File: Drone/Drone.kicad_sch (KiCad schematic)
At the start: 20 parts, among them IC1 STM32L412RBT6, J1 Conn_01x03_Pin, U1 ICP-10111, U2 BMI088

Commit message: new schematic
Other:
- added sheet Power (untitled.kicad_sch)
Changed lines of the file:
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@@
+		)
+	)
+	(sheet
+		(at 224.79 21.59)
+		(size 36.83 27.94)
+		(exclude_from_sim no)
+		(in_bom yes)
+		(on_board yes)
+		(dnp no)
+		(fields_autoplaced yes)
+		(stroke
+			(width 0.1524)
+			(type solid)
+		)
+		(fill
+			(color 0 0 0 0.0000)
+		)
+		(property "Sheetname" "Power"
+			(at 224.79 20.8784 0)
+			(effects
+				(font
+					(size 1.27 1.27)
+				)
+				(justify left bottom)
+			)
+		)
+		(property "Sheetfile" "untitled.kicad_sch"
+			(at 224.79 50.1146 0)
+			(effects
+				(font
+					(size 1.27 1.27)
+				)
+				(justify left top)
+			)
+		)
+		(instances
+			(project "Drone"
+				(path "/d78d7154-946a-48bf-8503-5b7bdc037515"
+					(page "2")
+				)
+			)
 		)
 	)

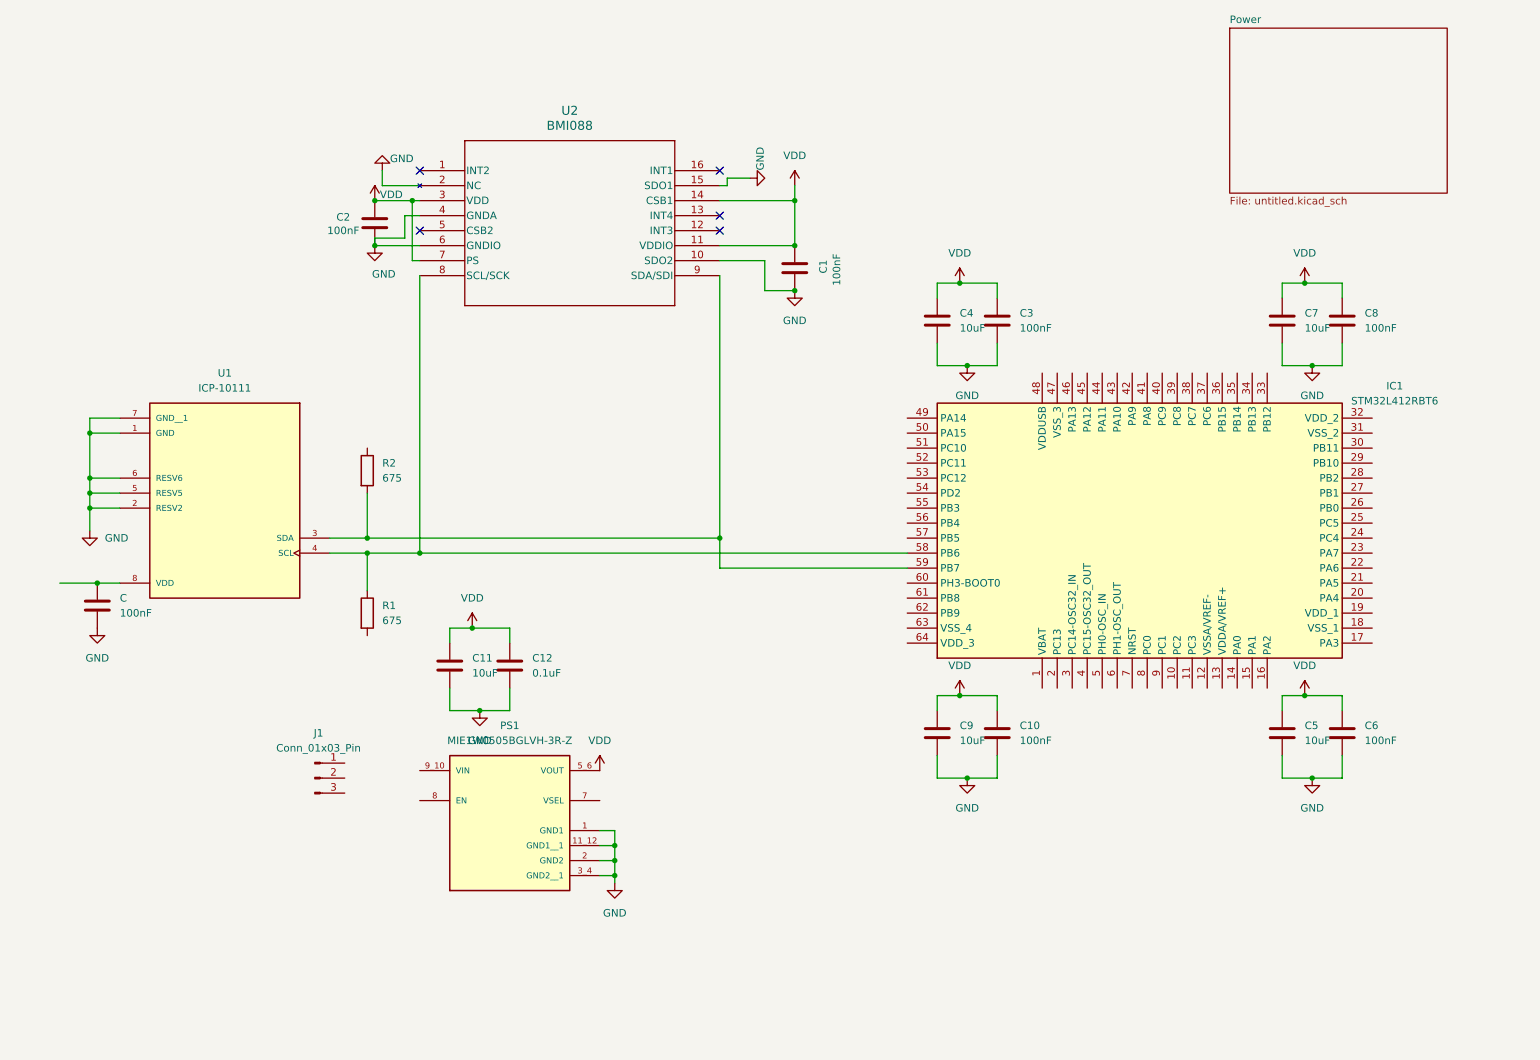
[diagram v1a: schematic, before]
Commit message: Added ICU and its connections to schematic
Added ICU and its connections to schematic
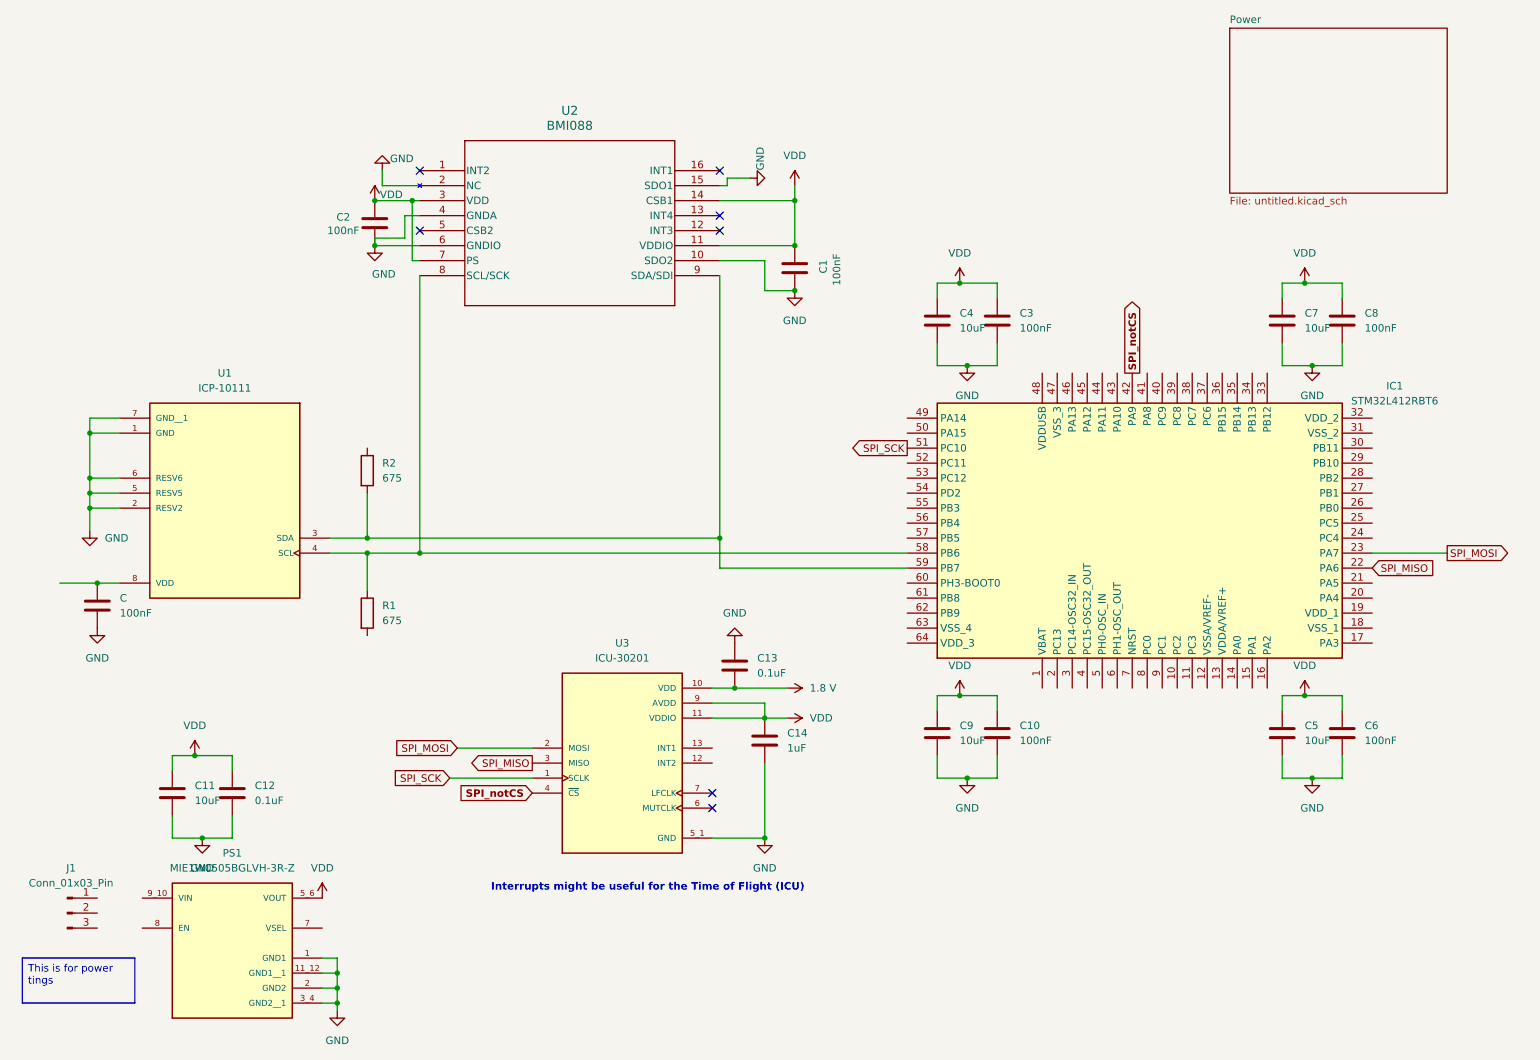
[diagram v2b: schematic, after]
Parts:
- added C13: 0.1uF, symbol Device:C
- added C14: 1uF, symbol Device:C
- added U3: ICU-30201, ICU-30201:XDCR_ICU-30201, symbol ICU-30201:ICU-30201
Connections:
- net GND: now also C13.1, C14.2, U3.5_1 (GND), U3.5_2 (GND), U3.8 (GND)
- net VDD: now also C14.1, U3.11 (VDDIO), U3.9 (AVDD)
- net SPI_MISO: now reaches IC1.22 (PA6)
- net SPI_MISO: now also U3.3 (MISO)
- net SPI_MOSI: now reaches IC1.23 (PA7)
- net SPI_MOSI: now also U3.2 (MOSI)
- net SPI_notCS: now reaches IC1.42 (PA9)
- net SPI_notCS: now also U3.4 (~{CS})
- net SPI_SCK: now reaches IC1.51 (PC10)
- net SPI_SCK: now also U3.1 (SCLK)
- new net 1.8 V: C13.2, U3.10 (VDD)
- no-connect marks 5 -> 7
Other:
- note added: "Interrupts might be useful for the Time of Flight (ICU)"
- moved on the sheet: C11, C12, J1, PS1

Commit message: added flashing stuff
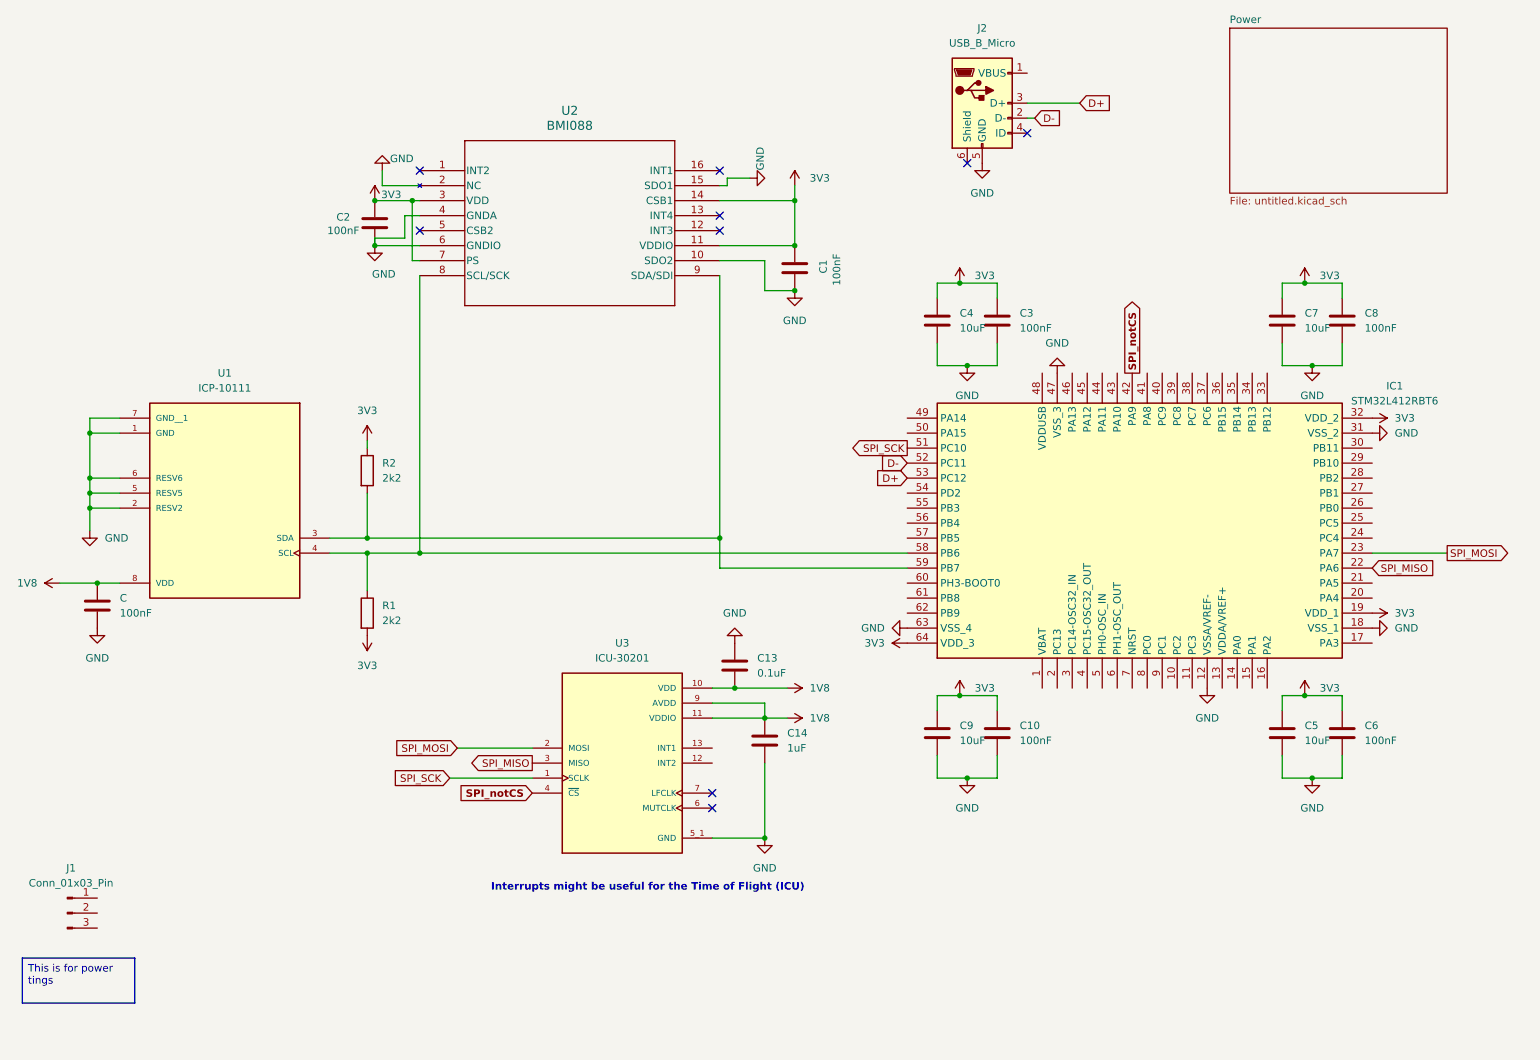
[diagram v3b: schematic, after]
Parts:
- removed C11: 10uF, symbol Device:C
- removed C12: 0.1uF, symbol Device:C
- removed PS1: MIE1W0505BGLVH-3R-Z, MIE1W0505BGLVH-3R-Z:CONV_MIE1W0505BGLVH-3R-Z, symbol DC-DC Converter:MIE1W0505BGLVH-3R-Z
- added J2: USB_B_Micro, symbol Connector:USB_B_Micro
- R1, R2: value 675 -> 2k2
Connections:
- net 1.8 V is gone; now on net 1V8: C13.2, U3.10 (VDD)
- net GND: now also IC1.12 (VSSA/VREF-), IC1.18 (VSS_1), IC1.31 (VSS_2), IC1.47 (VSS_3), IC1.63 (VSS_4), J2.5 (GND)
- net 1V8: now reaches C.1, U1.8 (VDD)
- net 1V8: now also C14.1, U3.11 (VDDIO), U3.9 (AVDD)
- net 3V3: now reaches R1.2
- net 3V3: now also C1.2, C10.1, C2.2, C3.1, C4.1, C5.1, C6.1, C7.1, C8.1, C9.1, IC1.19 (VDD_1), IC1.32 (VDD_2), IC1.64 (VDD_3), R2.1, U2.11 (VDDIO), U2.14 (CSB1), U2.3 (VDD), U2.7 (PS)
- net D-: now reaches IC1.52 (PC11)
- net D-: now also J2.2 (D-)
- net D+: now reaches IC1.53 (PC12)
- net D+: now also J2.3 (D+)
- removed net VDD: C1.2, C10.1, C14.1, C2.2, C3.1, C4.1, C5.1, C6.1, C7.1, C8.1, C9.1, U2.11 (VDDIO), U2.14 (CSB1), U2.3 (VDD), U2.7 (PS), U3.11 (VDDIO), U3.9 (AVDD)
- no-connect marks 7 -> 9
